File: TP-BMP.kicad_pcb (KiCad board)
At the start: 2 copper layers, 26 x 37 mm, 46 parts, among them P2 JST GH 10-pos, Q1 DMG1024UV-7, Q2 DMG1023UV-7, U1 TLV70233DBV, U2 74LVC2T45, U3 74LVC2T45, U4 74LVC2T45, U5 74LVC2T45, U6 STM32F103CBUx, Y1 8 MHz

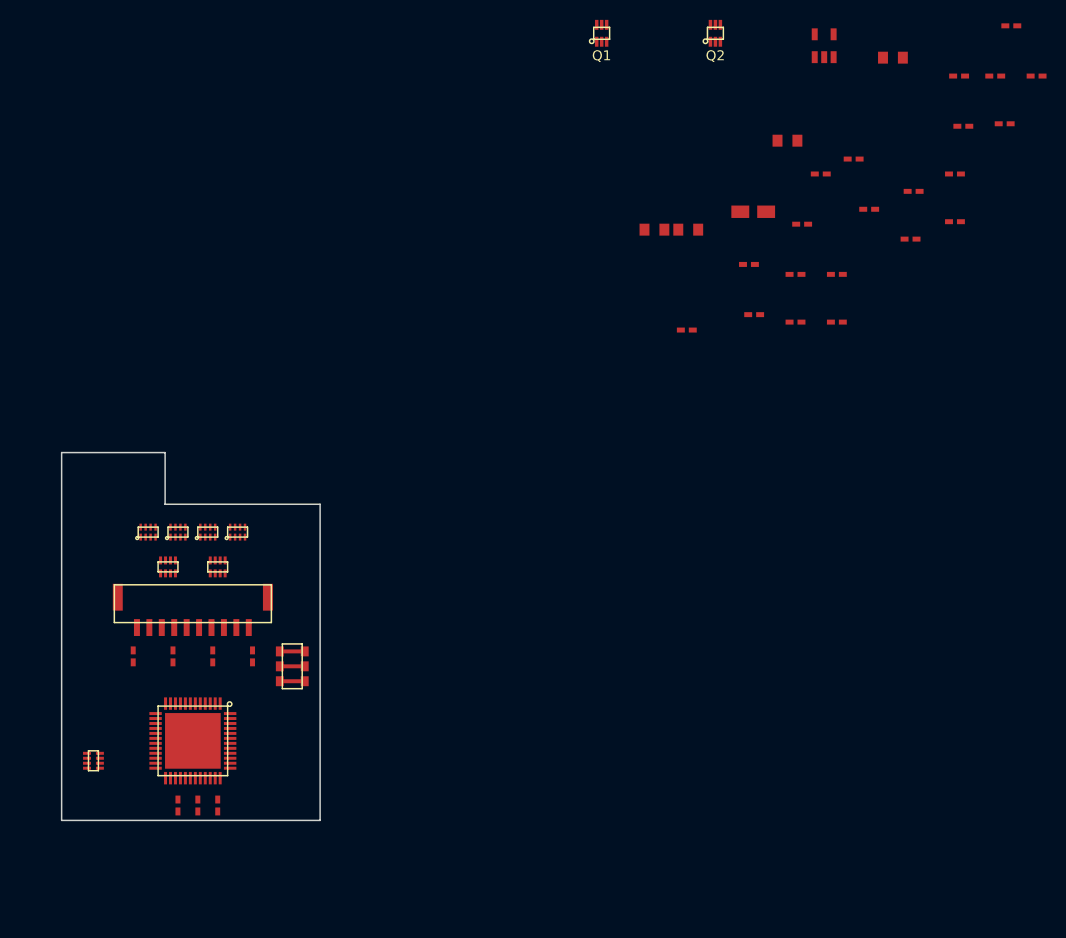
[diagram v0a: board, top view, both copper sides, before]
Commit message: Finished rev 0.1 PCB and ordered. Not yet tested. 4-layer design fit-checked with cardboard vs X220. Should be compatible with BMP v2.1.
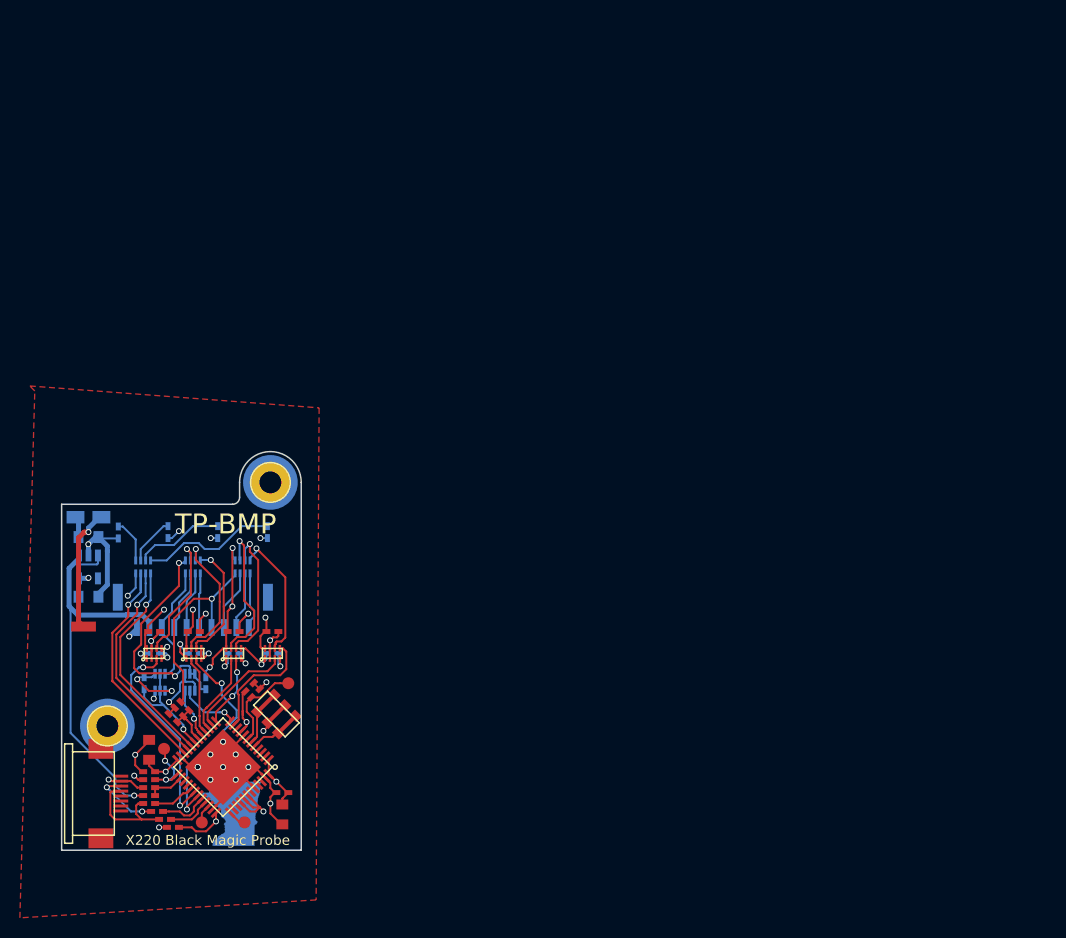
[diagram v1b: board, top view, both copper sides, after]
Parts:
- added G***: LOGO, KiCad_Footprints:ZF_LOGO_MN, B.Cu at (127.1, 137.9)
- added G***: LOGO, KiCad_Footprints:ZF_LOGO_OSHW, F.Cu at (117.4, 111.7)
- added P1: FPC, KiCad_Footprints:ZF_CONN_FPC_8POS_52745, F.Cu at (113.4, 136.1)
- added REF**: ZF_STRUCT_2-2_HOLE, KiCad_Footprints:ZF_STRUCT_2-2_HOLE, F.Cu at (131.2, 104.8)
- added REF**: ZF_STRUCT_2-2_HOLE, KiCad_Footprints:ZF_STRUCT_2-2_HOLE, F.Cu at (114.8, 129.3)
- added W1: SOLDER PAD, KiCad_Footprints:ZF_STRUCT_2.5x1, F.Cu at (112.4, 119.3)
- added W2: TEST PAD, KiCad_Footprints:ZF_CONN_1-2_pad, F.Cu at (133.0, 125.0)
- added W3: TEST PAD, KiCad_Footprints:ZF_CONN_1-2_pad, F.Cu at (124.3, 139.0)
- added W4: TEST PAD, KiCad_Footprints:ZF_CONN_1-2_pad, F.Cu at (128.6, 139.0)
- added W5: TEST PAD, KiCad_Footprints:ZF_CONN_1-2_pad, F.Cu at (120.5, 131.6)
- C1, C2, C3, C4, C5, C6, D1, D2, D3, D4, F1, P2, Q1, Q2, R1, R4, RN1, RN2, RN3, U1: moved to B.Cu
- moved R9 107.7 mm to (122.6, 127.3), turned to 135 degrees
- moved C18 107.4 mm to (122.0, 127.9), turned to 315 degrees
- moved C12 104.5 mm to (119.0, 133.9)
- moved R4 102.2 mm to (118.5, 125.0), turned to 270 degrees
- moved C2 97.4 mm to (112.9, 116.3)
- moved C8 92.9 mm to (127.5, 119.8)
- moved C10 91.7 mm to (131.4, 119.8)
- moved U1 90.7 mm to (112.9, 113.3)
- moved C9 89.3 mm to (123.5, 119.8)
- moved C5 88.0 mm to (123.5, 122.0)
- moved C15 87.7 mm to (132.4, 136.0)
- moved C13 86.9 mm to (121.4, 139.5)
- moved R8 86.2 mm to (119.0, 134.7), turned to 180 degrees
- moved Q2 85.9 mm to (120.1, 124.9)
- moved C7 85.7 mm to (119.5, 119.8)
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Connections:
- P2 pad 10: /RXD -> /TMS
- P2 pad 3: /TPWR -> /RST
- P2 pad 4: /RST -> /TXD
- P2 pad 5: /TDI -> /TDO
- P2 pad 6: /TDO -> /RXD
- P2 pad 7: /TCK -> /TPWR
- P2 pad 8: /TMS -> /TCK
- P2 pad 9: /TXD -> /TDI
- Q2 pad 3: /TPWR -> /RST
- RN1 pad 1: /LED0 -> +3V3
- RN1 pad 2: /LED1 -> /LED2
- RN1 pad 3: /LED2 -> /LED1
- RN1 pad 4: +3V3 -> /LED0
- RN1 pad 5: Net-(D1-Pad2) -> Net-(D4-Pad2)
- RN1 pad 6: Net-(D2-Pad2) -> Net-(D3-Pad2)
- RN1 pad 7: Net-(D3-Pad2) -> Net-(D2-Pad2)
- RN1 pad 8: Net-(D4-Pad2) -> Net-(D1-Pad2)
- RN2 pad 1: /xTPWR -> /xRXD
- RN2 pad 2: /xRST -> /xTDO
- RN2 pad 3: /xTDI -> /xTXD
- RN2 pad 4: /xTDO -> /xRST
- RN2 pad 5: /TDO -> /RST
- RN2 pad 6: /TDI -> /TXD
- RN2 pad 7: /RST -> /TDO
- RN2 pad 8: /TPWR -> /RXD
- RN3 pad 1: /xTCK -> /xTMS
- RN3 pad 2: /xTMS -> /xTDI
- RN3 pad 3: /xTXD -> /xTCK
- RN3 pad 4: /xRXD -> /xTPWR
- RN3 pad 5: /RXD -> /TPWR
- RN3 pad 6: /TXD -> /TCK
- RN3 pad 7: /TMS -> /TDI
- RN3 pad 8: /TCK -> /TMS
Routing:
- net GND: track 0.00 -> 81.1 mm, vias 0 -> 29
- net +3V3: track 0.00 -> 47.2 mm, vias 0 -> 14
- net +5V: track 0.00 -> 45.6 mm, vias 0 -> 1
- net /xTPWR: track 0.00 -> 39.2 mm, vias 0 -> 6
- net /LED2: track 0.00 -> 24.1 mm, vias 0 -> 1
- net /xRST: track 0.00 -> 23.4 mm, vias 0 -> 2
- net /LED1: track 0.00 -> 21.9 mm, vias 0 -> 1
- net /LED0: track 0.00 -> 21.6 mm, vias 0 -> 1
- net /iRXD: track 0.00 -> 21.2 mm, vias 0 -> 2
- net /TPWR: track 0.00 -> 21.2 mm, vias 0 -> 1
- net /iTXD: track 0.00 -> 20.8 mm, vias 0 -> 2
- net /xTCK: track 0.00 -> 14.8 mm, vias 0 -> 1
- net /xTDI: track 0.00 -> 14.1 mm, vias 0 -> 1
- net /xTDO: track 0.00 -> 13.9 mm, vias 0 -> 1
- net Net-(D4-Pad2): track 0.00 -> 13.8 mm
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- added copper zone on In2.Cu, net +3V3
- added copper zone on F.Cu, net GND
- added copper zone on In1.Cu, net GND
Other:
- board size 26 x 37 mm -> 24.1 x 40.1 mm
- copper layers 2 -> 4
- net class Default: trace_width 0.25 -> 0.2
- rule pad_to_mask_clearance: 0.2 -> 0
- board text added: "BACK SIDE = THUMBPRINT SCANNER CHIP (NOW JST CONNECTOR AND LEDS)"
- board text added: "KEYBOARD"
- board text added: "TP-BMP"
- board text added: "X220 Black Magic Probe"
- board text added: "git.io/v5kMk"
- board text added: "v0.1"
